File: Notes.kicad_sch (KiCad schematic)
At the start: 0 parts

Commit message: Interface Update
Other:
- company: (none) -> Peter Hancak
- title: (none) -> ESP32P4C5_BOARD
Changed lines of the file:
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@@
 	(generator_version "8.0")
 	(paper "A4")
+	(title_block
+		(title "ESP32P4C5_BOARD")
+		(date "2026-06-01")
+		(rev "A")
+		(company "Peter Hancak")
+	)
 	(text_box "CONTROLLED IMPEDANCE TRACE WIDTHS\n(Simulations done using ADS Controlled Impedance Line Designer)\n- Simulated is JLCPCB: JLC04161H-3313(Finished thickness1.56mm±10%)\n\n1. Microstrip Edge Coupled, 100 Ohm Differential Impedance, 0.35mm (center to center), 50mmm Length, f=1Ghz, Width = 0.1225 mm\n2. Coplanar Edge Coupled, 100 Ohm Differential Impedance, 0.35mm (center to center), 0.25mm Clearance, 50mmm Length, f=1Ghz, Width = 0.1354 mm, 0.35 - 0.1354 = 0.2146 mm (edge to edge spacing)\n3. USB Coplanar Edge Coupled, 90 Ohm Differential Impedance, 0.5mm (center to center), 0.25mm Clearance, 50mmm Length, f=240Mhz, Width = 0.1704 mm, 0.5 - 0.1704 = 0.3296 mm\n4. USB Microstrip Edge Coupled, 90 Ohm Differential Impedance, 0.5mm (center to center), 50mmm Length, f=240Mhz, Width = 0.1722 mm\n\nRF TRACE 50 Ohm\n- Coplanar single-ended , f is 2.5 GHz, L 20mm, Clearance 0.25mm, Width = 0.1472 mm\n- Coplanar single-ended , f is 5 GHz, L 20mm, Clearance 0.25mm, Width = 0.1475 mm\n\n\nSMA CONNECTOR SIGNAL PIN (MIDDLE) FOOTPRINT\n- With normal 0.35 mm clearance resulted in a veryy significant signal degradation\n- I recalculated the clearance for the middle pin using ADS:\n  - Coplanar Single-Ended, Length: 5mm, Width: 1.37 mmm (width of the pin), f: 5GHz, Clearance = 0.4046 mm\n  \n\nINTERFACE NOTES:\n- SPI2 IOMUX, DMA\n- SPI3 GPIOMATRIX, NODMA\n- I2S1 GPIOMATRIX\n- I2S2 GPIOMATRIX\n- I2C0 GPIOMATRIX CSI and P4 to C5\n- I2C1 GPIOMATRIX External Interface\n- UART0 IOMUX DEBUG\n- UART1 IOMUX External Interface\n- UART2\n- UART3\n- UART4\n- I3C\n- PARLIO\n  - PSSI_PDCK (Parallel Data Clock) to parlio_tx_clk_pad_out\n  - PSSI_RDY (Ready / Flow Control) to \n  - PSSI_DE (Data Enable) to parlio_tx_data15_pad_out MSB\n  - PSSI_D0 through PSSI_D7 (8-bit Data Bus) to parlio_tx_data0_pad_out 0 to 7\n  Connect suitable pins to the PSSI/SPI header then setup pins with ESP32P4 signals\n- DSI (LCD)\n  - LCD Choice: CTP ST7701S FT5316 D310FPC9362 CST128 (MIPI 2 LANE)\n- SDIO\n  - HS Communication between the P4 and C5 (Slave)\n  - INT pin deddicated as interrupt from C5 to P4 (Not part of SDIO)\n\nSERIES TERMINATION\n- CSI, DSI, SDIO (near P4), UART0, UART1, NOT I2C\nSDIO\n- Array Series termination on SDIO DATA 0-3\n- Individual series termination on CLK, CMD\n- PU on the SDIO INT (Interrupt) pin (Open Drain)"
 		(exclude_from_sim no)
@@
 		(exclude_from_sim no)
 		(at 27.305 29.845 0)
-		(size 77.851 36.703)
+		(size 77.851 49.403)
 		(stroke
 			(width 0)
@@
 		)
 	)
-	(text_box "ESP32P4 HARDWARE CONSIDERATIONS:\n- The P4 does have a USB connector\n  - \n- BOOT CONFIGURATION\n  - \n\n- CSI_LDO-CE Pin on the CAMERA turns the internal camera LDO ON or OFF thereby alowing the chip to turn it off when not needed (in sleep mode)\n- CSI_FLASH-LED pin is a CAMERA output pinn that is designed to send ouput signal to a flash to iluminate the surounding at the exact time of image capture\n  (Will not be used NC) "
+	(text_box "ESP32P4 HARDWARE CONSIDERATIONS:\n- DEBUG\n  - The P4 has both USB ports exposed and the UART0 as a last resort debug.\n  - Main flash/debug is to be done through the USB/JTAG port\n  - The MCU JTAG pins are exposed on a header but do not include the PU and PD resistors.\n- BOOT CONFIGURATION\n  - \n\n- CSI_LDO-CE Pin on the CAMERA turns the internal camera LDO ON or OFF thereby alowing the chip to turn it off when not needed (in sleep mode)\n- CSI_FLASH-LED pin is a CAMERA output pinn that is designed to send ouput signal to a flash to iluminate the surounding at the exact time of image capture\n  (Will not be used NC)\n\n- RESET CIRCUT\n  - The goal is for the ESP32P4 to reset from global reset pin, but also to reset after a firmware update without causing global reset of other devices.\n  - Implementation: GLOBAL RESET is connected through a buffer to the MCU that only pulls reset LOW and is HIGH-Z otherwise. The MCU RST (PU) pin is exposed with the JTAG pins on a headder to allow RST after upload."
 		(exclude_from_sim no)
 		(at 27.178 149.86 0)
@@
 		)
 	)
-	(text_box "ESP32P4 SETUP NOTES:\n1. The PARLIO (Parallel interface) pins are set as general PARLIO IO to be set up with specific pin functtiin throuugh the GPIO Matrix. The function of each PARLIO pin can be determined based on the target device.\n2. GPIO45 is to be set up as CINT (SDIO Interrupt) for the ESP32C5 to let the P4 know of available information on the SDIO bus.\n3. The W25Q256JWPIQ flash memory is a 1.8V device and is powered as well as logic I/O from VDDO_FLASH (PIN71). Set up logic 1.8V output before connecting. Set the EFUSE_0PXA_TIEH_SEL_0 register.\n   (DO NOT solder on the flash until the flash votage is set to 1.8V)\n4. VDD_HP_n is CORE power with 1.3V MAX. Set to 1.2V (as per reference)\n"
+	(text_box "ESP32P4 SETUP NOTES:\n1. The PARLIO (Parallel interface) pins are set as general PARLIO IO to be set up with specific pin functtiin throuugh the GPIO Matrix. The function of each PARLIO pin can be determined based on the target device.\n2. GPIO45 is to be set up as CINT (SDIO Interrupt) for the ESP32C5 to let the P4 know of available information on the SDIO bus.\n3. The W25Q256JWPIQ flash memory is a 1.8V device and is powered as well as logic I/O from VDDO_FLASH (PIN71). Set up logic 1.8V output before connecting. Set the EFUSE_0PXA_TIEH_SEL_0 register.\n   (DO NOT solder on the flash until the flash votage is set to 1.8V)\n4. VDD_HP_n is CORE power with 1.3V MAX. Set to 1.2V (as per reference)\n5. BOOT CONFIGURATION\n   - The ESP32P4 can be programmed using USB-Serial-JTAG Download\n     (The USB Serial/JTAG Controller is able to put the ESP32-P4 into download mode automatically - NO NEED TO PULL GPIO35 LOW MANUALLY)\n   - GPIO35 HIGH: SPI Boot mode (default), PU is permanently on GPIO35\n   - GPIO35 LOW: Joint Download Boot mode (USB-Serial-JTAG Download Boot, UART Download Boot, SPI Slave Download Boot, USB 2.0 OTG Download)\n   - JTAG Signal Source Control\n     - eFuse 3: EFUSE_JTAG_SEL_ENABLE to 1\n     - GPIO34 can be used for JTAG signal source\n       - 1: JTAG signals come from USB Serial/JTAG Controller\n       - 0: JTAG signals come from corresponding pins MTDI, MTCK, MTMS, and MTDO\n\n"
 		(exclude_from_sim no)
 		(at 194.564 99.314 0)
@@
 	(text_box "PROJECT REQUIREMENTS/GOALS:\n- Camera OV5647 to capture real-time vide (or smiliar)\n- Provide WIFI link (to transmit the real-time video)\n- Control motor through CAN-FD interface\n- High Speed 8-bit pparallel connection to expansion PCBs\n- High Speed USB connector\n- I2C, UART, SPI (through FPC) interfaces\n\nSECONDARY GOALS:\n- Function as a simple server\n- Motor control through PWM pins\n- LCD with touch screen (MIPI 2LANE)\n"
 		(exclude_from_sim no)
-		(at 27.432 69.85 0)
-		(size 77.724 40.64)
+		(at 27.432 85.09 0)
+		(size 77.724 25.4)
 		(stroke
 			(width 0)

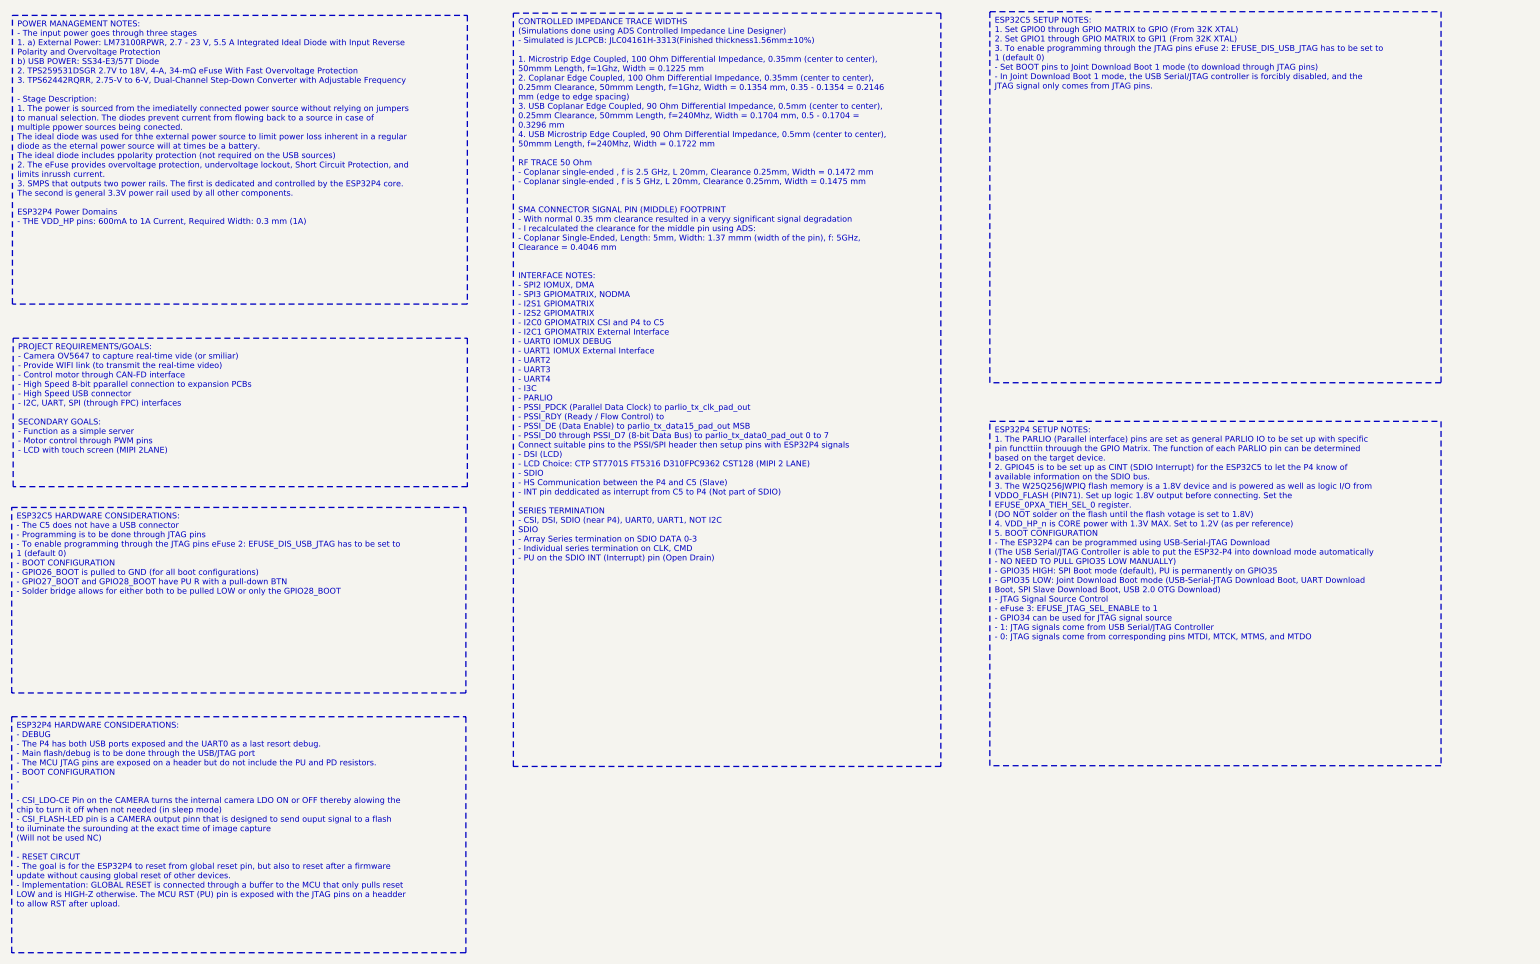
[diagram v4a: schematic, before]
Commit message: Small trace layout fixes
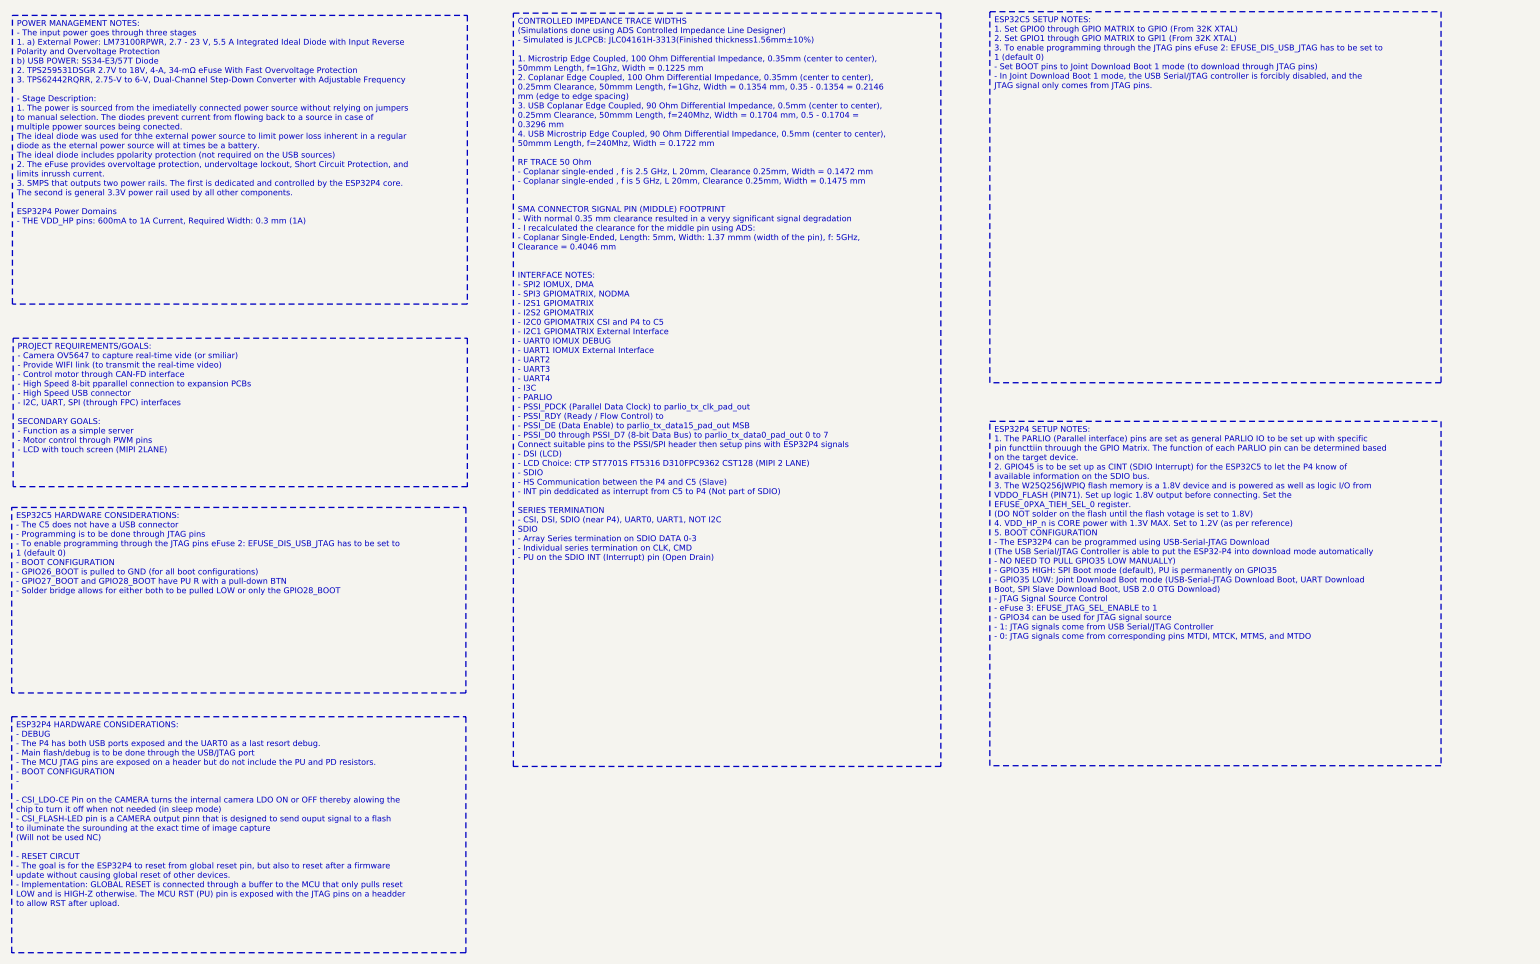
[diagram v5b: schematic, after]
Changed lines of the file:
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@@
 (kicad_sch
-	(version 20231120)
+	(version 20260306)
 	(generator "eeschema")
-	(generator_version "8.0")
+	(generator_version "10.0")
 	(paper "A4")
 	(title_block
@@
 		(at 113.03 29.464 0)
 		(size 73.152 128.905)
+		(margins 0.75 0.75 0.75 0.75)
 		(stroke
 			(width 0)
@@
 		(at 27.305 29.845 0)
 		(size 77.851 49.403)
+		(margins 0.75 0.75 0.75 0.75)
 		(stroke
 			(width 0)
@@
 		(at 194.564 29.21 0)
 		(size 77.216 63.5)
+		(margins 0.75 0.75 0.75 0.75)
 		(stroke
 			(width 0)
@@
 		(at 27.178 149.86 0)
 		(size 77.724 40.386)
+		(margins 0.75 0.75 0.75 0.75)
 		(stroke
 			(width 0)
@@
 		(at 27.178 114.046 0)
 		(size 77.724 31.75)
+		(margins 0.75 0.75 0.75 0.75)
 		(stroke
 			(width 0)
@@
 		(at 194.564 99.314 0)
 		(size 77.216 58.928)
+		(margins 0.75 0.75 0.75 0.75)
 		(stroke
 			(width 0)
@@
 		(at 27.432 85.09 0)
 		(size 77.724 25.4)
+		(margins 0.75 0.75 0.75 0.75)
 		(stroke
 			(width 0)

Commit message: Power rail update
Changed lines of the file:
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@@
 		)
 	)
-	(text_box "POWER MANAGEMENT NOTES:\n- The input power goes through three stages \n  1. a) External Power: LM73100RPWR, 2.7 - 23 V, 5.5 A Integrated Ideal Diode with Input Reverse Polarity and Overvoltage Protection\n     b) USB POWER: SS34-E3/57T Diode\n  2. TPS259531DSGR 2.7V to 18V, 4-A, 34-mΩ eFuse With Fast Overvoltage Protection\n  3. TPS62442RQRR, 2.75-V to 6-V, Dual-Channel Step-Down Converter with Adjustable Frequency\n\n- Stage Description:\n  1. The power is sourced from the imediatelly connected power source without relying on jumpers to manual selection. The diodes prevent current from flowing back to a source in case of multiple ppower sources being conected.\n     The ideal diode was used for thhe external power source to limit power loss inherent in a regular diode as the eternal power source will at times be a battery.   \n     The ideal diode includes ppolarity protection (not required on the USB sources)\n  2. The eFuse provides overvoltage protection, undervoltage lockout, Short Circuit Protection, and limits inrussh current.\n  3. SMPS that outputs two power rails. The first is dedicated and controlled by the ESP32P4 core. The second is general 3.3V power rail used by all other components.\n\nESP32P4 Power Domains\n- THE VDD_HP pins: 600mA to 1A Current, Required Width: 0.3 mm (1A)"
+	(text_box "POWER MANAGEMENT NOTES:\n- The input power goes through three stages \n  1. a) External Power: LM73100RPWR, 2.7 - 23 V, 5.5 A Integrated Ideal Diode with Input Reverse Polarity and Overvoltage Protection\n     b) USB POWER: SS34-E3/57T Diode\n  2. TPS259531DSGR 2.7V to 18V, 4-A, 34-mΩ eFuse With Fast Overvoltage Protection\n  3. TPS62442RQRR, 2.75-V to 6-V, Dual-Channel Step-Down Converter with Adjustable Frequency\n\n- Stage Description:\n  1. The power is sourced from the imediatelly connected power source without relying on jumpers to manual selection. The diodes prevent current from flowing back to a source in case of multiple ppower sources being conected.\n     The ideal diode was used for thhe external power source to limit power loss inherent in a regular diode as the eternal power source will at times be a battery.   \n     The ideal diode includes ppolarity protection (not required on the USB sources)\n  2. The eFuse provides overvoltage protection, undervoltage lockout, Short Circuit Protection, and limits inrussh current.\n  3. SMPS that outputs two power rails. The first is dedicated and controlled by the ESP32P4 core. The second is general 3.3V power rail used by all other components.\n\nESP32P4 Power Domains\n- THE VDD_HP pins: 600mA to 1A Current, Required Width: 0.3 mm (1A)\n\nIdeal Diode LM73100RPWR Parameter Notes:\n- Maximum System Peak Current (IOUT): 2.5 A (to cleanly capture joint ESP32 radio bursts, camera operations, and converter losses).\n- I IMON = 2.5 A×181 μA/A=452.5 μA (181 μA/A from data sheet, how much current goes through IMON pin for each 1A useful OUT current)  \n- LM73100RPWR will be monitoring for 425.5 μA\n- Calculate the Value for RIMON = VADC_MAX/IIMON = 3.3 V/452.5 μA ≈ 7.29 kΩ IMON\n​\nEFUSE TPS259531DSGR Notes:\n- Over Voltage Clamp (OVC) set at 5.7V (for TPS25953x)\n\nSMPS TPS62442RQRR Notes:\n- The PG1 and PG2 left floatng as they are not used. The MCU PU pins are handled through a parallel C. \n"
 		(exclude_from_sim no)
 		(at 27.305 29.845 0)
-		(size 77.851 49.403)
+		(size 77.851 65.4049)
 		(margins 0.75 0.75 0.75 0.75)
 		(stroke
@@
 		)
 	)
-	(text_box "ESP32P4 HARDWARE CONSIDERATIONS:\n- DEBUG\n  - The P4 has both USB ports exposed and the UART0 as a last resort debug.\n  - Main flash/debug is to be done through the USB/JTAG port\n  - The MCU JTAG pins are exposed on a header but do not include the PU and PD resistors.\n- BOOT CONFIGURATION\n  - \n\n- CSI_LDO-CE Pin on the CAMERA turns the internal camera LDO ON or OFF thereby alowing the chip to turn it off when not needed (in sleep mode)\n- CSI_FLASH-LED pin is a CAMERA output pinn that is designed to send ouput signal to a flash to iluminate the surounding at the exact time of image capture\n  (Will not be used NC)\n\n- RESET CIRCUT\n  - The goal is for the ESP32P4 to reset from global reset pin, but also to reset after a firmware update without causing global reset of other devices.\n  - Implementation: GLOBAL RESET is connected through a buffer to the MCU that only pulls reset LOW and is HIGH-Z otherwise. The MCU RST (PU) pin is exposed with the JTAG pins on a headder to allow RST after upload."
+	(text_box "ESP32P4 HARDWARE CONSIDERATIONS:\n- DEBUG\n  - The P4 has both USB ports exposed and the UART0 as a last resort debug.\n  - Main flash/debug is to be done through the USB/JTAG port\n  - The MCU JTAG pins are exposed on a header but do not include the PU and PD resistors.\n- BOOT CONFIGURATION\n  - \n\n- CSI_LDO-CE Pin on the CAMERA turns the internal camera LDO ON or OFF thereby alowing the chip to turn it off when not needed (in sleep mode)\n- CSI_FLASH-LED pin is a CAMERA output pinn that is designed to send ouput signal to a flash to iluminate the surounding at the exact time of image capture\n  (Will not be used NC)\n\n- RESET CIRCUT\n  - The goal is for the ESP32P4 to reset from global reset pin, but also to reset after a firmware update without causing global reset of other devices.\n  - Implementation: GLOBAL RESET is connected through a buffer to the MCU that only pulls reset LOW and is HIGH-Z otherwise. The MCU RST (PU) pin is exposed with the JTAG pins on a headder to allow RST after upload.\n  - PU (RST) Timing Considerations: The PU has to stay low for tSTBL = 50uS after VIN stable at 3.3V\n    - Place a 100nF capacitor at PU."
 		(exclude_from_sim no)
 		(at 27.178 149.86 0)
@@
 	(text_box "ESP32C5 HARDWARE CONSIDERATIONS:\n- The C5 does not have a USB connector\n  - Programming is to be done through JTAG pins\n  - To enable programming through the JTAG pins eFuse 2: EFUSE_DIS_USB_JTAG has to be set to 1 (default 0)\n- BOOT CONFIGURATION\n  - GPIO26_BOOT is pulled to GND (for all boot configurations) \n  - GPIO27_BOOT and GPIO28_BOOT have PU R with a pull-down BTN\n  - Solder bridge allows for either both to be pulled LOW or only the GPIO28_BOOT"
 		(exclude_from_sim no)
-		(at 27.178 114.046 0)
-		(size 77.724 31.75)
+		(at 27.178 123.19 0)
+		(size 77.724 22.606)
 		(margins 0.75 0.75 0.75 0.75)
 		(stroke
@@
 	(text_box "PROJECT REQUIREMENTS/GOALS:\n- Camera OV5647 to capture real-time vide (or smiliar)\n- Provide WIFI link (to transmit the real-time video)\n- Control motor through CAN-FD interface\n- High Speed 8-bit pparallel connection to expansion PCBs\n- High Speed USB connector\n- I2C, UART, SPI (through FPC) interfaces\n\nSECONDARY GOALS:\n- Function as a simple server\n- Motor control through PWM pins\n- LCD with touch screen (MIPI 2LANE)\n"
 		(exclude_from_sim no)
-		(at 27.432 85.09 0)
-		(size 77.724 25.4)
+		(at 27.432 97.79 0)
+		(size 77.724 21.59)
 		(margins 0.75 0.75 0.75 0.75)
 		(stroke
